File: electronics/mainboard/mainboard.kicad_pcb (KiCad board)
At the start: 2 copper layers, 4 parts

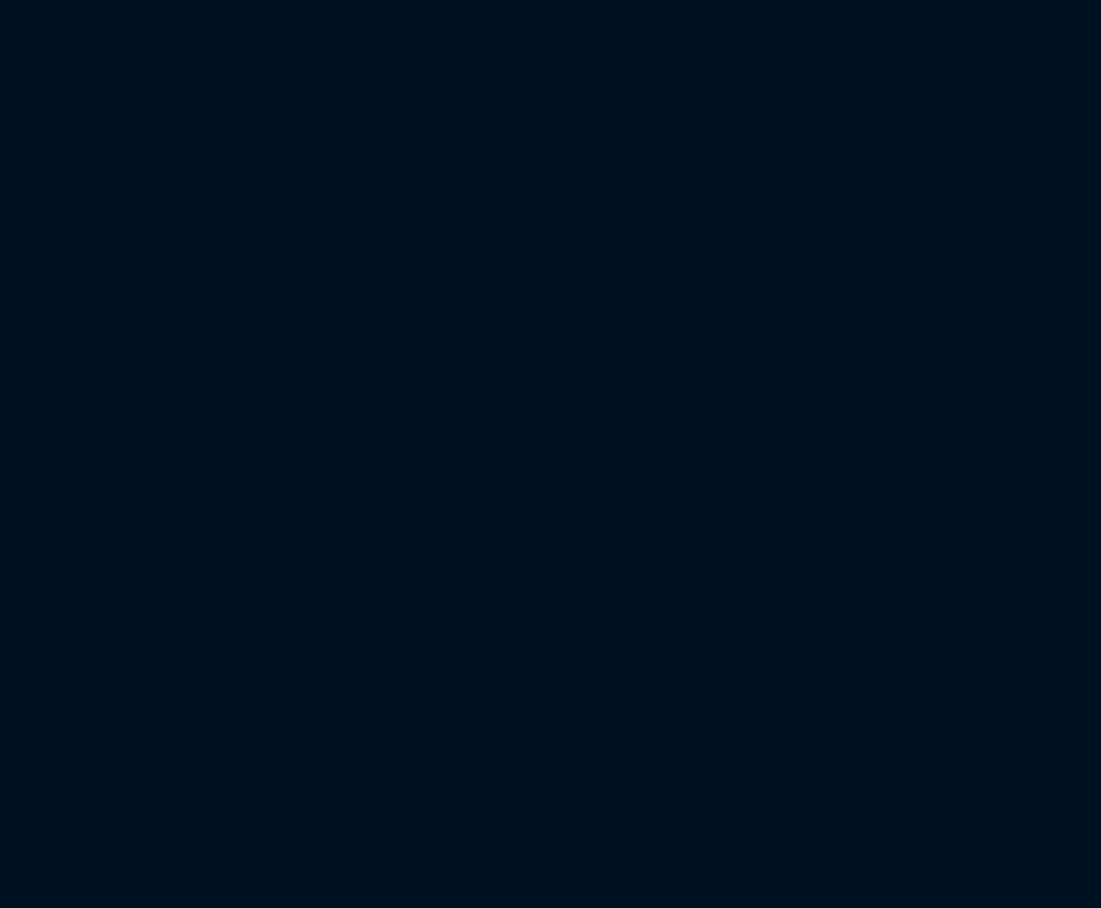
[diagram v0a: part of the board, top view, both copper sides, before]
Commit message: finished power subcircuit and made netlist
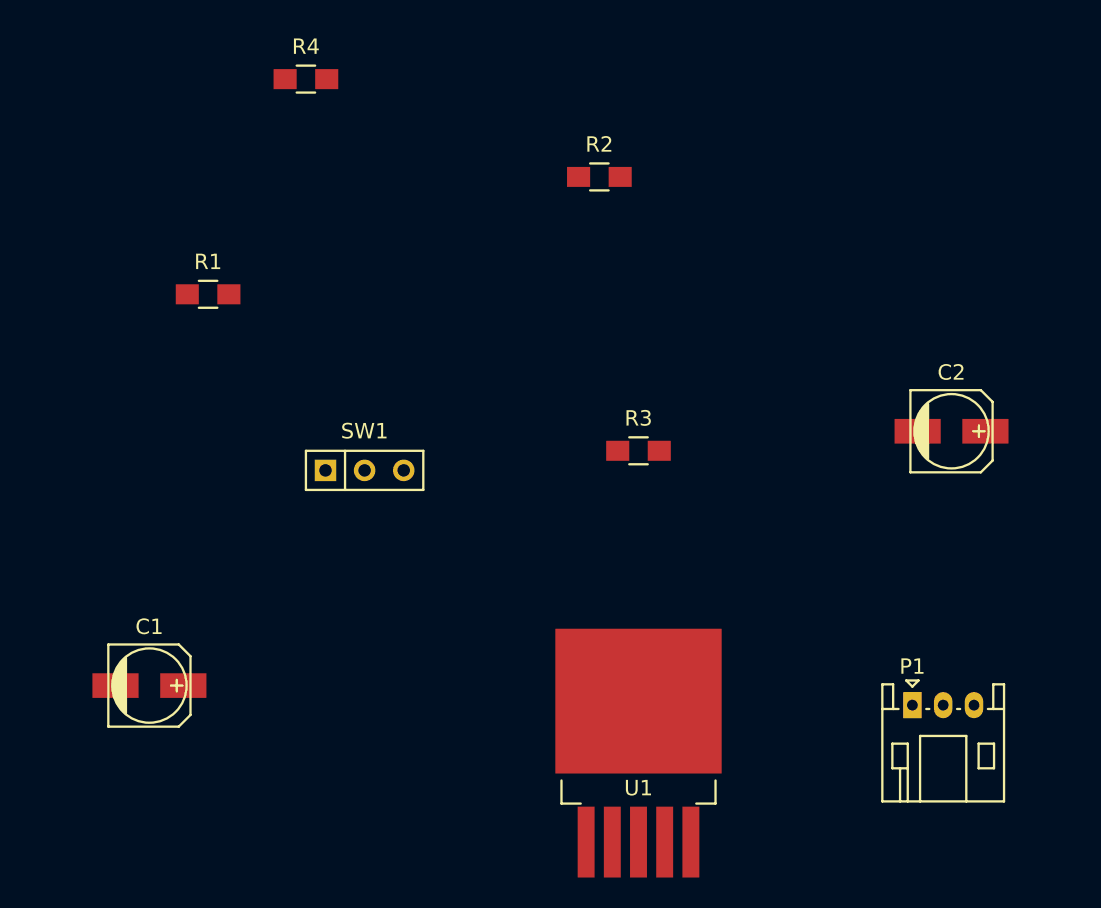
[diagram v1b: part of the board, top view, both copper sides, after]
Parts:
- added C1: 10uF, Capacitors_SMD:c_elec_5x5.3, F.Cu at (119.4, 101.6)
- added C2: 22uF, Capacitors_SMD:c_elec_5x5.3, F.Cu at (171.4, 85.1)
- added P1: CONN_01X03, Connectors_JST:JST_PH_S3B-PH-K_03x2.00mm_Angled, F.Cu at (168.9, 102.9)
- added R1: 100K, Resistors_SMD:R_0805_HandSoldering, F.Cu at (123.2, 76.2)
- added R2: 100K, Resistors_SMD:R_0805_HandSoldering, F.Cu at (148.6, 68.6)
- added R3: 33K, Resistors_SMD:R_0805_HandSoldering, F.Cu at (151.1, 86.4)
- added R4: 15K, Resistors_SMD:R_0805_HandSoldering, F.Cu at (129.5, 62.2)
- added SW1: SWITCH_INV, Buttons_Switches_ThroughHole:SW_Micro_SPST, F.Cu at (133.3, 87.6)
- added U1: MIC29312, TO_SOT_Packages_SMD:TO-263-5Lead, F.Cu at (151.1, 111.8)
